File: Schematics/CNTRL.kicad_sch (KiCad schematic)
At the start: 46 parts, among them SW1 RotaryEncoder_Switch, SW2 RotaryEncoder_Switch, SW3 RotaryEncoder_Switch, SW4 RotaryEncoder_Switch, U6 PCA9555PW

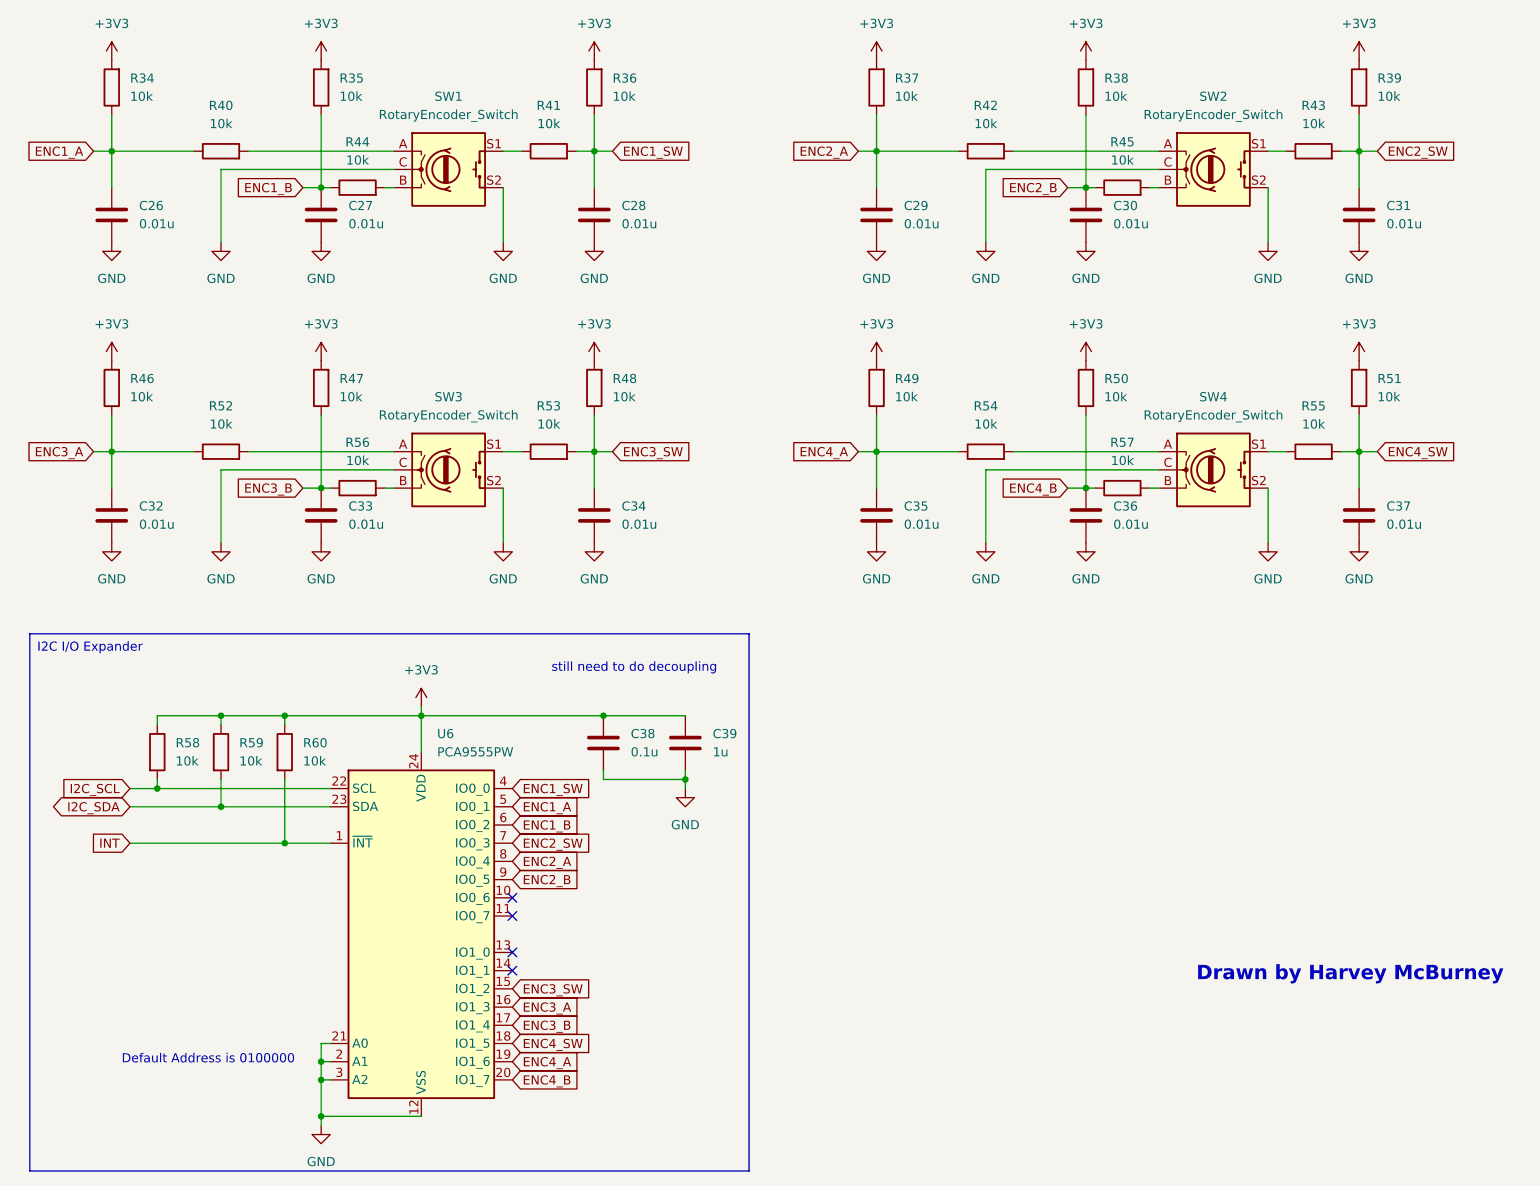
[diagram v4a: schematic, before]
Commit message: Updated to KiCAD v9
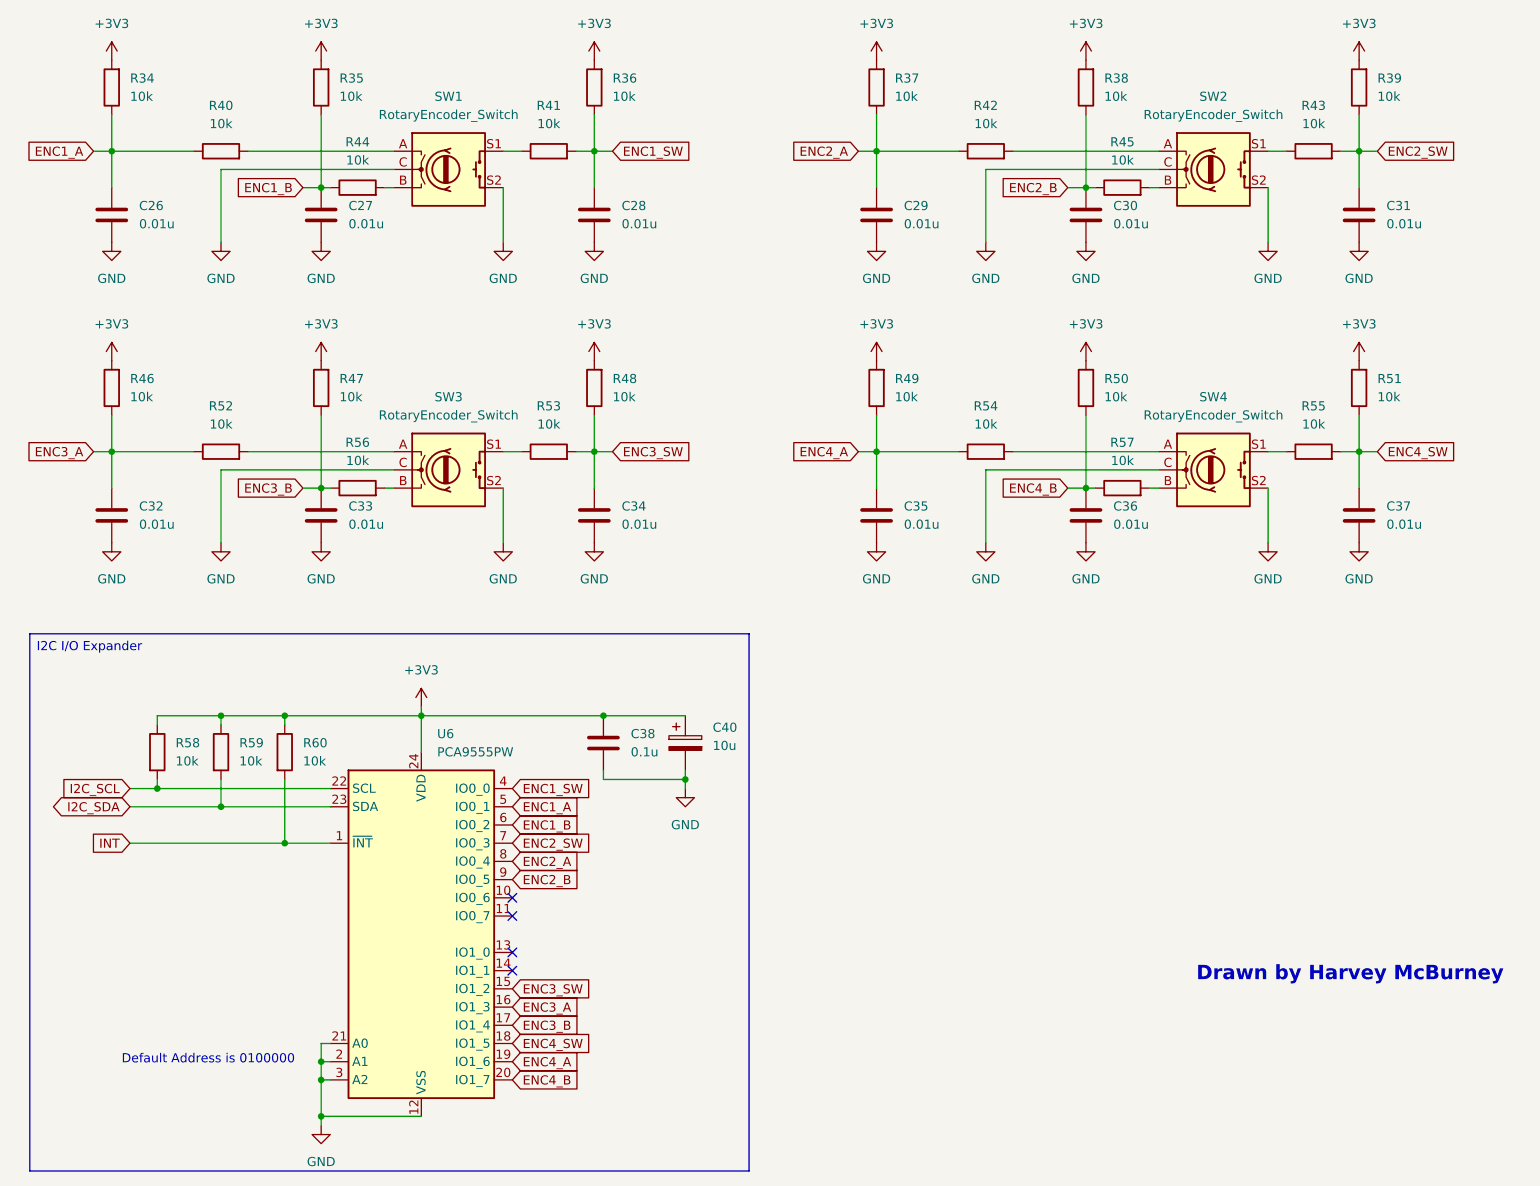
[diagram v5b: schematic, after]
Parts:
- removed C39: 1u, symbol Device:C
- added C40: 10u, Capacitor_SMD:CP_Elec_5x5.4, symbol Device:C_Polarized
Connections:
- net +3V3: now also C40.1
- net GND: now also C40.2
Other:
- note removed: "still need to do decoupling"
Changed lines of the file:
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@@
 (kicad_sch
-	(version 20231120)
+	(version 20250114)
 	(generator "eeschema")
-	(generator_version "8.0")
+	(generator_version "9.0")
 	(paper "A4")
 	(title_block
@@
 		(date "2025-02-12")
 	)
+	(text "Default Address is 0100000"
+		(exclude_from_sim no)
+		(at 40.132 181.356 0)
+		(effects
+			(font
+				(size 1.27 1.27)
+			)
+		)
+	)
+	(text "Drawn by Harvey McBurney"
+		(exclude_from_sim no)
+		(at 199.39 169.418 0)
+		(effects
+			(font
+				(size 2 2)
+				(thickness 0.6)
+				(bold yes)
+			)
+		)
+	)
+	(text_box "I2C I/O Expander"
+		(exclude_from_sim no)
+		(at 15.24 121.92 0)
+		(size 100.33 74.93)
+		(margins 0.9525 0.9525 0.9525 0.9525)
+		(stroke
+			(width 0)
+			(type default)
+		)
+		(fill
+			(type none)
+		)
+		(effects
+			(font
+				(size 1.27 1.27)
+			)
+			(justify left top)
+		)
+	)
 	(junction
 		(at 55.88 101.6)
@@
 		)
 	)
-	(text_box "I2C I/O Expander"
-		(exclude_from_sim no)
-		(at 15.24 121.92 0)
-		(size 100.33 74.93)
-		(stroke
-			(width 0)
-			(type default)
-		)
-		(fill
-			(type none)
-		)
-		(effects
-			(font
-				(size 1.27 1.27)
-			)
-			(justify left top)
-		)
-	)
-	(text "Default Address is 0100000"
-		(exclude_from_sim no)
-		(at 40.132 181.356 0)
-		(effects
-			(font
-				(size 1.27 1.27)
-			)
-		)
-	)
-	(text "still need to do decoupling"
-		(exclude_from_sim no)
-		(at 99.568 126.746 0)
-		(effects
-			(font
-				(size 1.27 1.27)
-			)
-		)
-	)
-	(text "Drawn by Harvey McBurney"
-		(exclude_from_sim no)
-		(at 199.39 169.418 0)
-		(effects
-			(font
-				(size 2 2)
-				(thickness 0.6)
-				(bold yes)
-			)
-		)
-	)
 	(global_label "ENC1_SW"
 		(shape input)
@@
 	)
 	(symbol
-		(lib_id "Device:C")
-		(at 106.68 137.16 0)
-		(unit 1)
-		(exclude_from_sim no)
-		(in_bom yes)
-		(on_board yes)
-		(dnp no)
-		(fields_autoplaced yes)
-		(property "Reference" "C39"
-			(at 110.49 135.8899 0)
-			(effects
-				(font
-					(size 1.27 1.27)
-				)
-				(justify left)
-			)
-		)
-		(property "Value" "1u"
-			(at 110.49 138.4299 0)
-			(effects
-				(font
-					(size 1.27 1.27)
-				)
-				(justify left)
-			)
-		)
-		(property "Footprint" ""
-			(at 107.6452 140.97 0)
-			(effects
-				(font
-					(size 1.27 1.27)
-				)
-				(hide yes)
-			)
-		)
-		(property "Datasheet" "~"
-			(at 106.68 137.16 0)
-			(effects
-				(font
-					(size 1.27 1.27)
-				)
-				(hide yes)
-			)
-		)
-		(property "Description" "Unpolarized capacitor"
-			(at 106.68 137.16 0)
-			(effects
-				(font
-					(size 1.27 1.27)
-				)
-				(hide yes)
-			)
-		)
-		(pin "1"
-		)
-		(pin "2"
-		)
-		(instances
-			(project "Harmoniser HAT"
-				(path "/41751dd2-97f9-4cc6-b9e6-b561e5949053/5d678f4e-03b5-43f5-b100-a64e850a5e5c"
-					(reference "C39")
-					(unit 1)
-				)
-			)
-		)
-	)
-	(symbol
 		(lib_id "power:GND")
 		(at 148.59 67.31 0)
@@
 					(unit 1)
 				)
+			)
+		)
+	)
+	(symbol
+		(lib_id "Device:C_Polarized")
+		(at 106.68 137.16 0)
+		(unit 1)
+		(exclude_from_sim no)
+		(in_bom yes)
+		(on_board yes)
+		(dnp no)
+		(fields_autoplaced yes)
+		(property "Reference" "C40"
+			(at 110.49 135.0009 0)
+			(effects
+				(font
+					(size 1.27 1.27)
+				)
+				(justify left)
+			)
+		)
+		(property "Value" "10u"
+			(at 110.49 137.5409 0)
+			(effects
+				(font
+					(size 1.27 1.27)
+				)
+				(justify left)
+			)
+		)
+		(property "Footprint" "Capacitor_SMD:CP_Elec_5x5.4"
+			(at 107.6452 140.97 0)
+			(effects
+				(font
+					(size 1.27 1.27)
+				)
+				(hide yes)
+			)
+		)
+		(property "Datasheet" "~"
+			(at 106.68 137.16 0)
+			(effects
+				(font
+					(size 1.27 1.27)
+				)
+				(hide yes)
+			)
+		)
+		(property "Description" "Polarized capacitor"
+			(at 106.68 137.16 0)
+			(effects
+				(font
+					(size 1.27 1.27)
+				)
+				(hide yes)
+			)
+		)
+		(pin "1"
+		)
+		(pin "2"
+		)
+		(instances
+			(project "Harmoniser HAT"
+				(path "/41751dd2-97f9-4cc6-b9e6-b561e5949053/5d678f4e-03b5-43f5-b100-a64e850a5e5c"
+					(reference "C40")
+					(unit 1)
+				)
